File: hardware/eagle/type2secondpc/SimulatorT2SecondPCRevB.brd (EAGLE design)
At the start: 48.3 x 48.3 mm, 5 parts

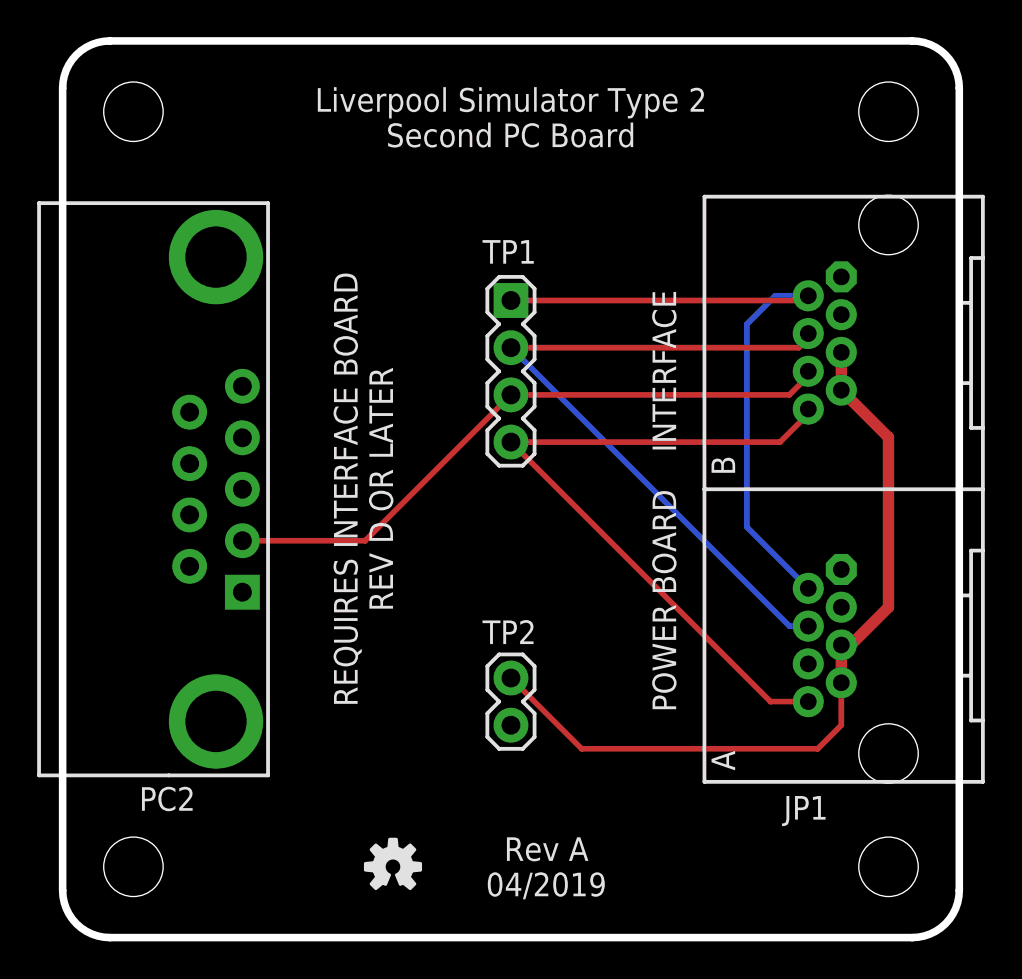
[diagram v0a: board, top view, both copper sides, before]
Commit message: Enhanced surge protection
Power Rev D, 2nd PC Rev B boards with improved surge protection,
Gerbers, Cost Estimation tool, New enclosure drilling templates.
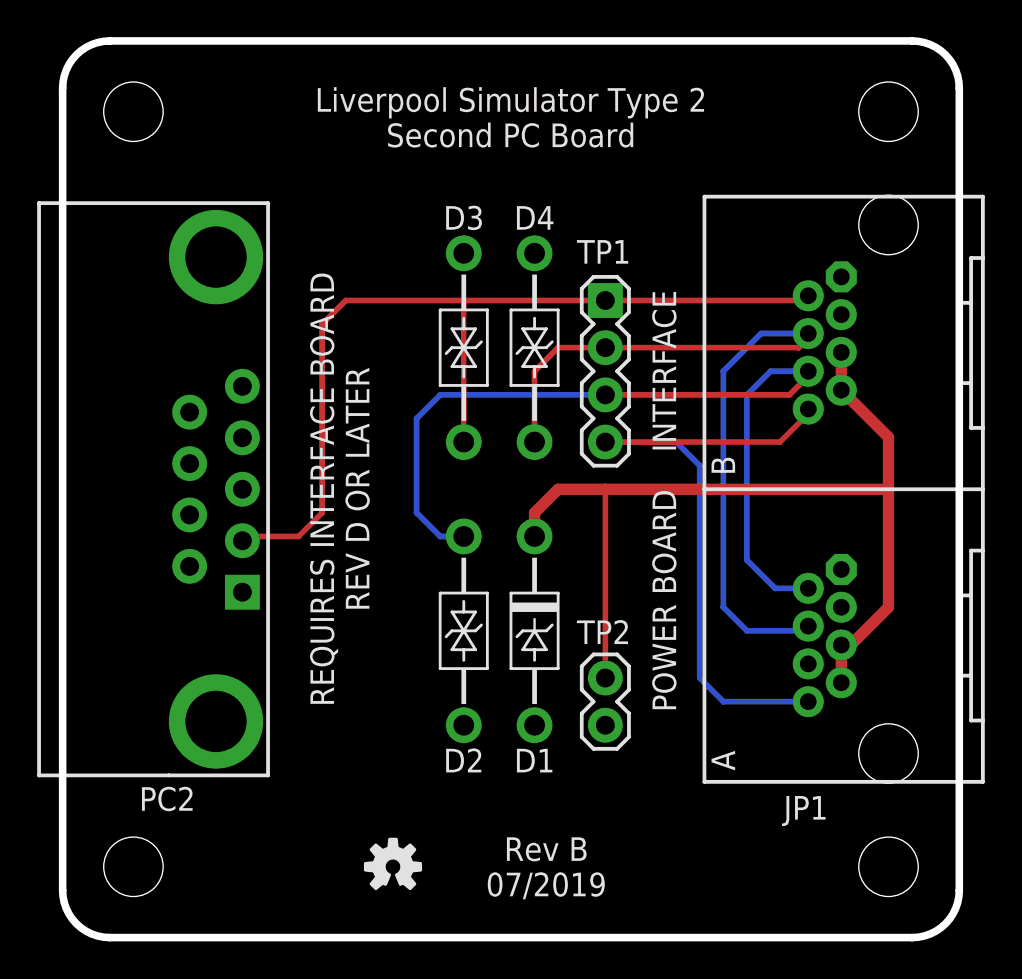
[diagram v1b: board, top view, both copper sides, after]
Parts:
- added D1: SA12A, AIC_Custom:DO41_TVS_UNI
- added D2, D3, D4: SA15CA, AIC_Custom:DO41_TVS_BI
- moved TP1 5.08 mm to (29.2, 34.3)
- moved TP2 5.08 mm to (29.2, 14.0)
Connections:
- net GND: now also D1.ANODE, D2.A, D3.A, D4.A
- net RXD: now also D4.C
- net TX2: now also D2.C, JP1.A2; no longer PC2.2
- net TXD: now also D3.C, PC2.2; no longer JP1.A2
- net VIN2: now also D1.CATHODE
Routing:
- net TXD: track 35.6 -> 49.5 mm
- net TX2: track 34.4 -> 47.1 mm
- net VIN2: track 42.4 -> 51.2 mm
- net RXD: track 38.7 -> 42.8 mm
- net P8: track 38.7 -> 35.2 mm
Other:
- board text added: "Rev B 07/2019"
- board text removed: "Rev A 04/2019"
